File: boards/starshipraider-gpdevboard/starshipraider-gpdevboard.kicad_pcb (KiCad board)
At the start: 4 copper layers, 55 x 42 mm, 68 parts, among them J1 STARSHIPRAIDER_IOBOARD_MODULE, J2 GREENPAK_DEVKIT_HDR, P1 MMCX, P2 MMCX, P3 CONN_01X02, U1 74LVC1T45, U10 74LVC1T45, U11 74LVC1T45, U12 74LVC1T45, U13 74LVC1T45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

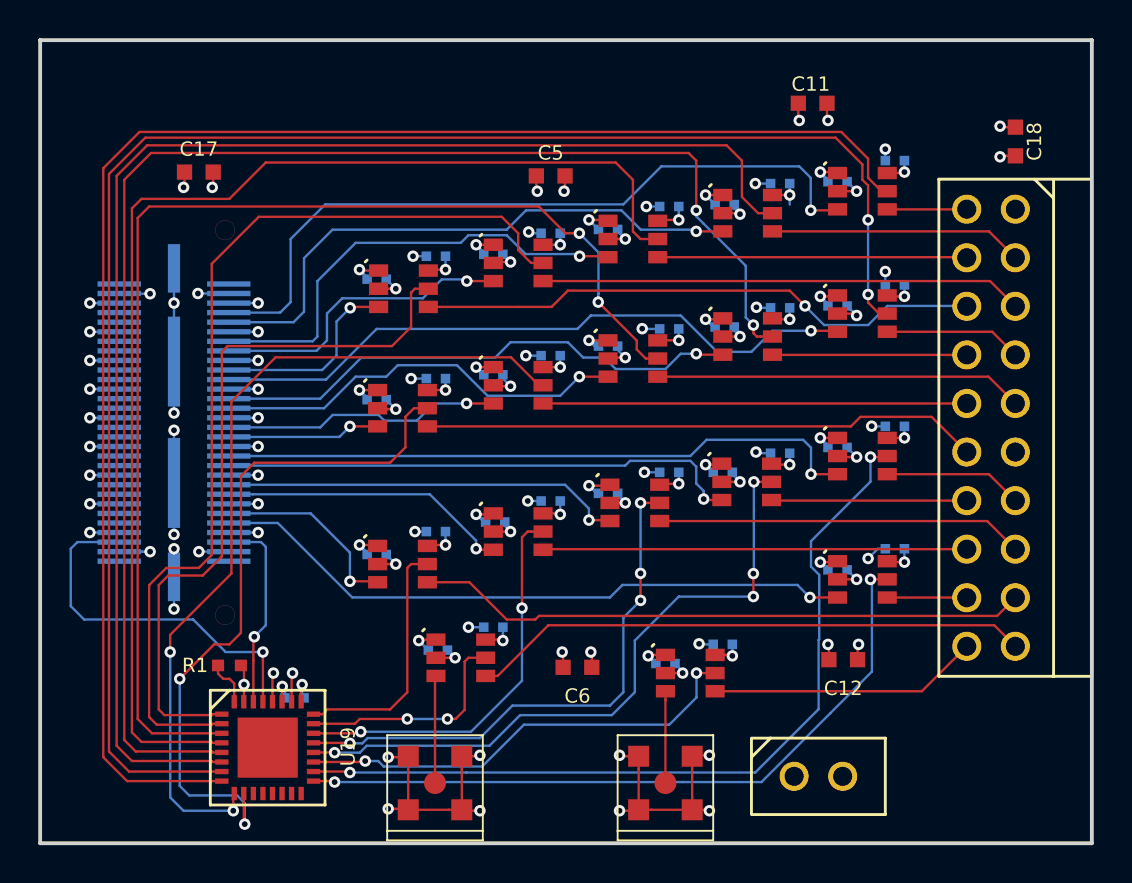
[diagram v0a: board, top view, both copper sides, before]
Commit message: Various layout tweaks during design review
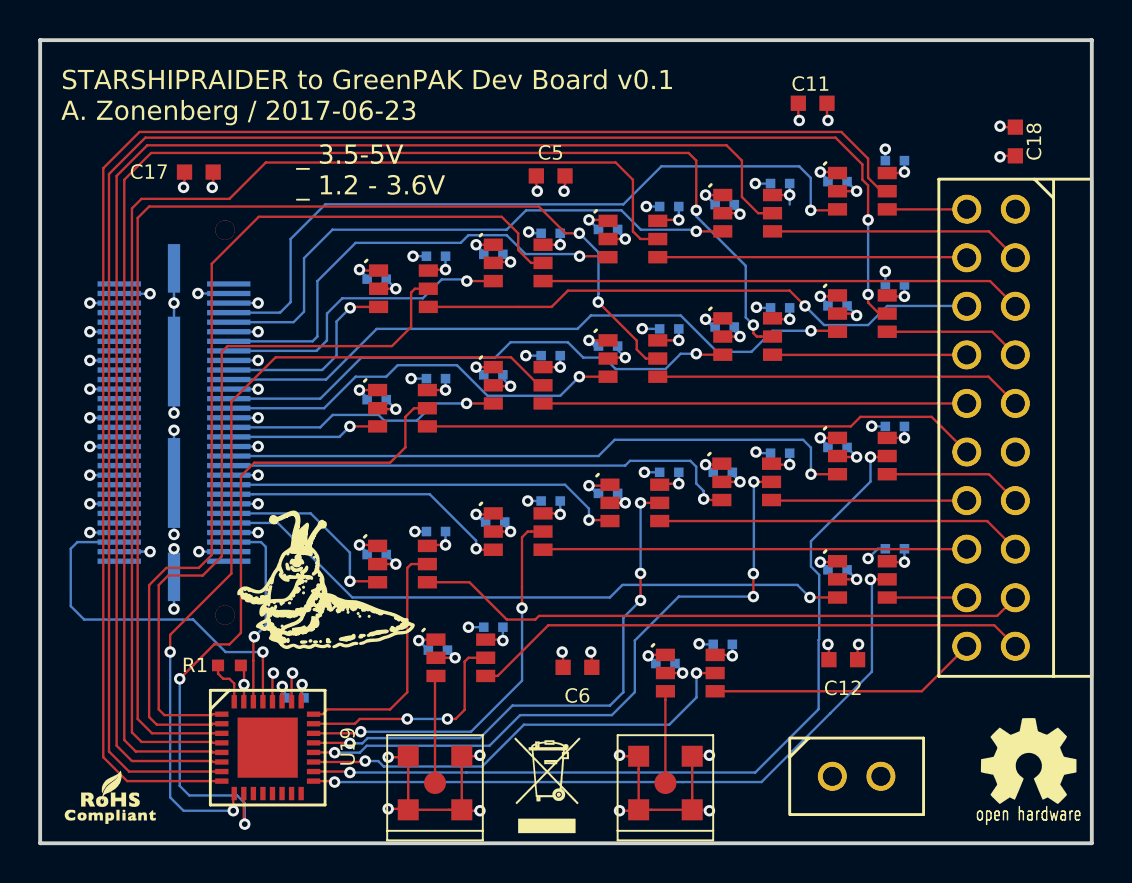
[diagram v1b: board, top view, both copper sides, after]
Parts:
- added G***: LOGO, azonenberg_pcb:LONGTHING-1200DPI, F.Cu at (33.5, 45.6)
- added G***: LOGO, w_logo:Logo_silk_WEEE_3.4x5mm, F.Cu at (44.5, 56.0)
- added G***: LOGO, w_logo:Logo_silk_ROHS_5x2.8mm, F.Cu at (21.7, 56.6)
- added G***: LOGO, w_logo:Logo_silk_OSHW_6x6mm, F.Cu at (69.7, 54.7)
- moved P3 2.00 mm to (60.7, 55.5)
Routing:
- net /VCCO_GP: track 179.6 -> 179.0 mm
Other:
- board text added: "STARSHIPRAIDER to GreenPAK Dev Board v0.1 A. Zonenberg / 2017-06-23"
- board text added: "_ 3.5-5V _ 1.2 - 3.6V"
